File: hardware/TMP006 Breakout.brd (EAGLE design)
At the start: 20.3 x 20.3 mm, 14 parts, among them U1 TMP006

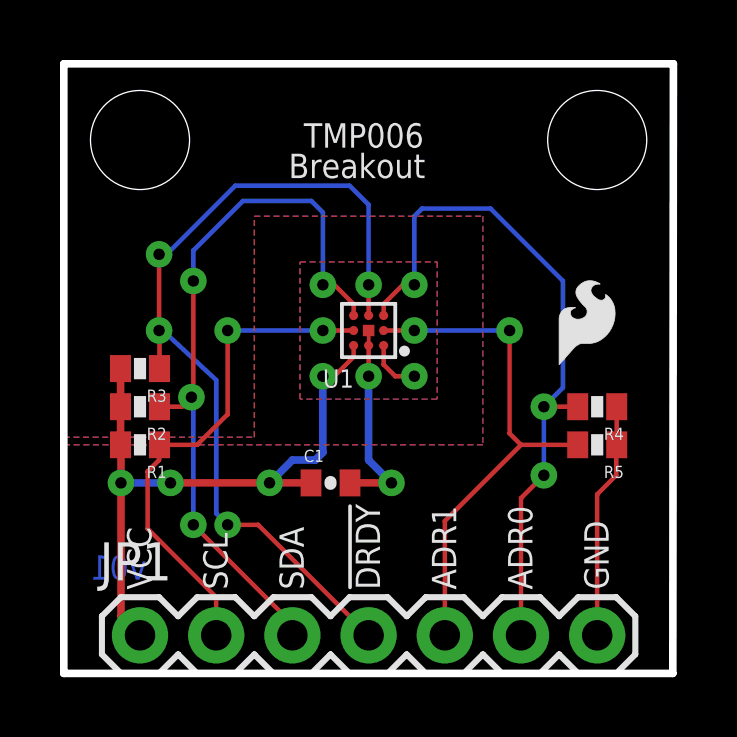
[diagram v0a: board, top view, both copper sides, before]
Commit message: Updates to v01: 402 -> 603 packages, added trestrict, changed trace sizes.
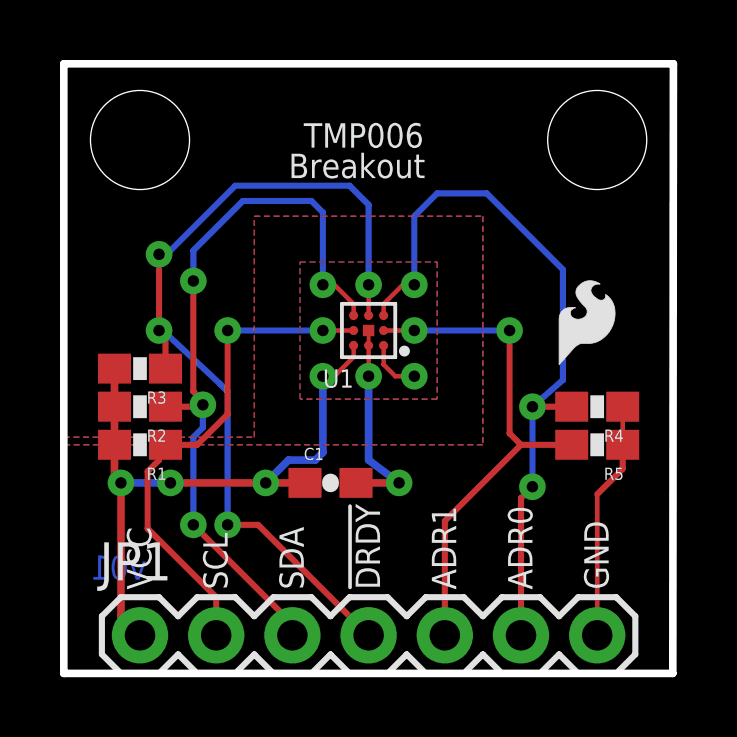
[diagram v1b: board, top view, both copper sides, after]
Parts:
- C1: device SparkFun-Capacitors:0402-CAP -> SparkFun-Capacitors:0603-CAP
- R1, R2, R3, R4, R5: device SparkFun-Resistors:0402-RES -> SparkFun-Resistors:0603-RES
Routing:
- net ADR0: track 23.5 -> 24.4 mm
- net GND: track 16.0 -> 16.5 mm
